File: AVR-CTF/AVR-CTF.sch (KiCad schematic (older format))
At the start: 0 parts

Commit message: Esquematico para revision
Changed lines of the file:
@@
 F0 "power_supply" 50
 F1 "power_supply.sch" 50
+F2 "VBUS" I R 3000 3500 50
 $EndSheet
 $Sheet
-S 3200 2000 1200 1700
+S 4500 2000 1200 1700
 U 621FB334
 F0 "MONITOR" 50
 F1 "MONITOR.sch" 50
+F2 "T_MCU_RX" I L 4500 2125 50
+F3 "T_MCU_TX" I L 4500 2225 50
+F4 "T_MCU_SDA" O L 4500 2450 50
+F5 "T_MCU_SCL" O L 4500 2550 50
 $EndSheet
 $Sheet
-S 4600 2000 1200 1700
+S 3150 2000 1200 1700
 U 6220499D
 F0 "MCU" 50
 F1 "MCU.sch" 50
+F2 "T_MCU_RX" I R 4350 2125 50
+F3 "T_MCU_TX" I R 4350 2225 50
+F4 "T_MCU_SDA" O R 4350 2450 50
+F5 "T_MCU_SCL" O R 4350 2550 50
+F6 "VBUS" I L 3150 3500 50
 $EndSheet
+Wire Wire Line
+	4350 2125 4500 2125
+Wire Wire Line
+	4350 2225 4500 2225
+Wire Wire Line
+	4350 2450 4500 2450
+Wire Wire Line
+	4350 2550 4500 2550
+Wire Wire Line
+	3000 3500 3150 3500
 $EndSCHEMATC

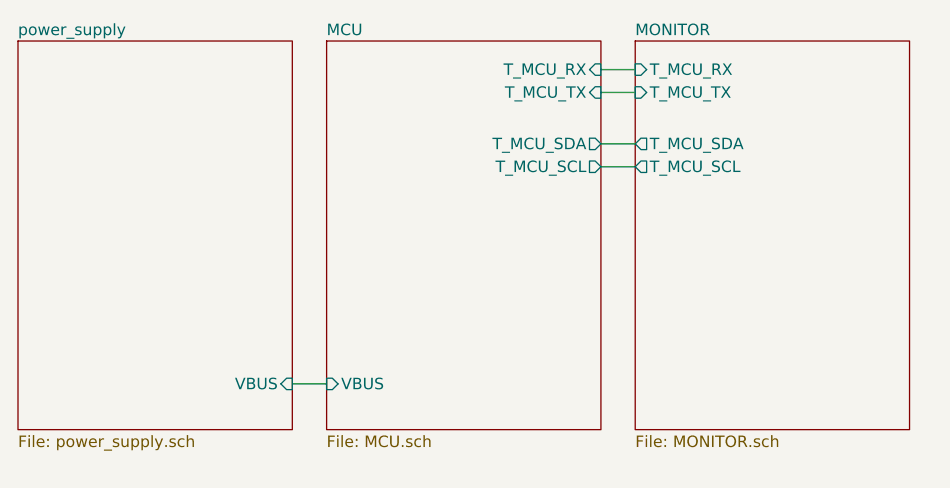
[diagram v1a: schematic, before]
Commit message: Anexo de otro FTDI y regulador de voltaje
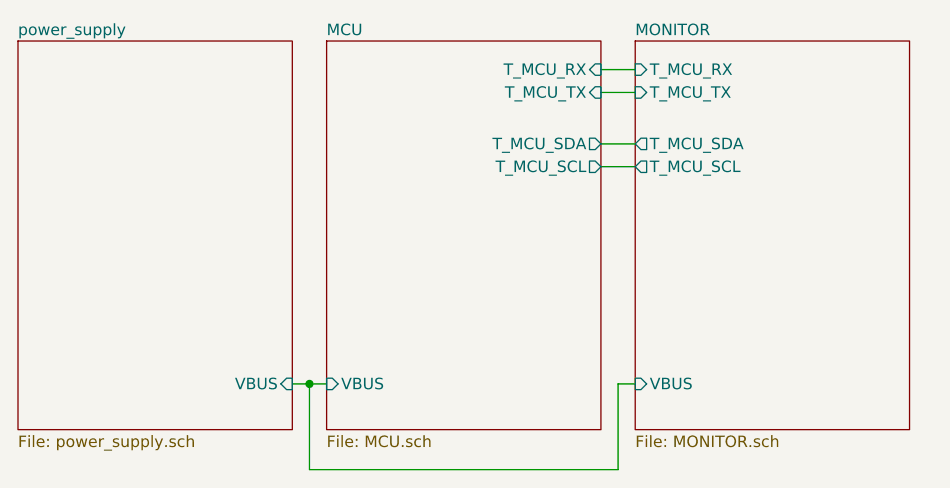
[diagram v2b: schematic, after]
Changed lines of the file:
@@
 F4 "T_MCU_SDA" O L 4500 2450 50
 F5 "T_MCU_SCL" O L 4500 2550 50
+F6 "VBUS" I L 4500 3500 50
 $EndSheet
 $Sheet
@@
 	4350 2550 4500 2550
 Wire Wire Line
-	3000 3500 3150 3500
+	3000 3500 3075 3500
+Wire Wire Line
+	3075 3500 3075 3875
+Wire Wire Line
+	3075 3875 4425 3875
+Wire Wire Line
+	4425 3875 4425 3500
+Wire Wire Line
+	4425 3500 4500 3500
+Connection ~ 3075 3500
+Wire Wire Line
+	3075 3500 3150 3500
 $EndSCHEMATC
